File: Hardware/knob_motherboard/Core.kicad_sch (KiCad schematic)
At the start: 20 parts, among them J2 Conn_01x14_Socket, J3 Conn_ARM_SWD_TagConnect_TC203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, U1 ESP32-S3-WROOM-1U, Y2 Crystal_Small

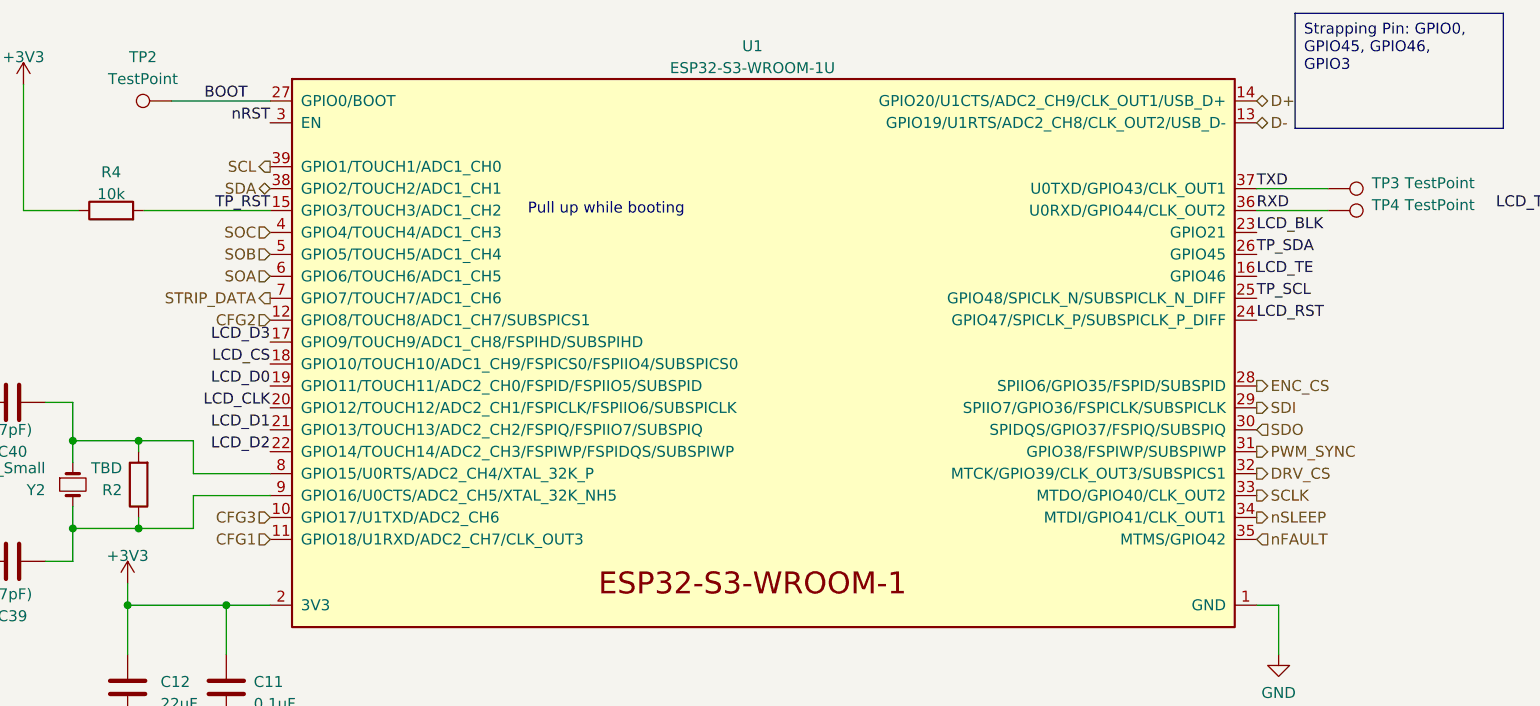
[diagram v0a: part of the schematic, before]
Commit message: drv8311 spi bugfix & ch224k CFG1 bugfix
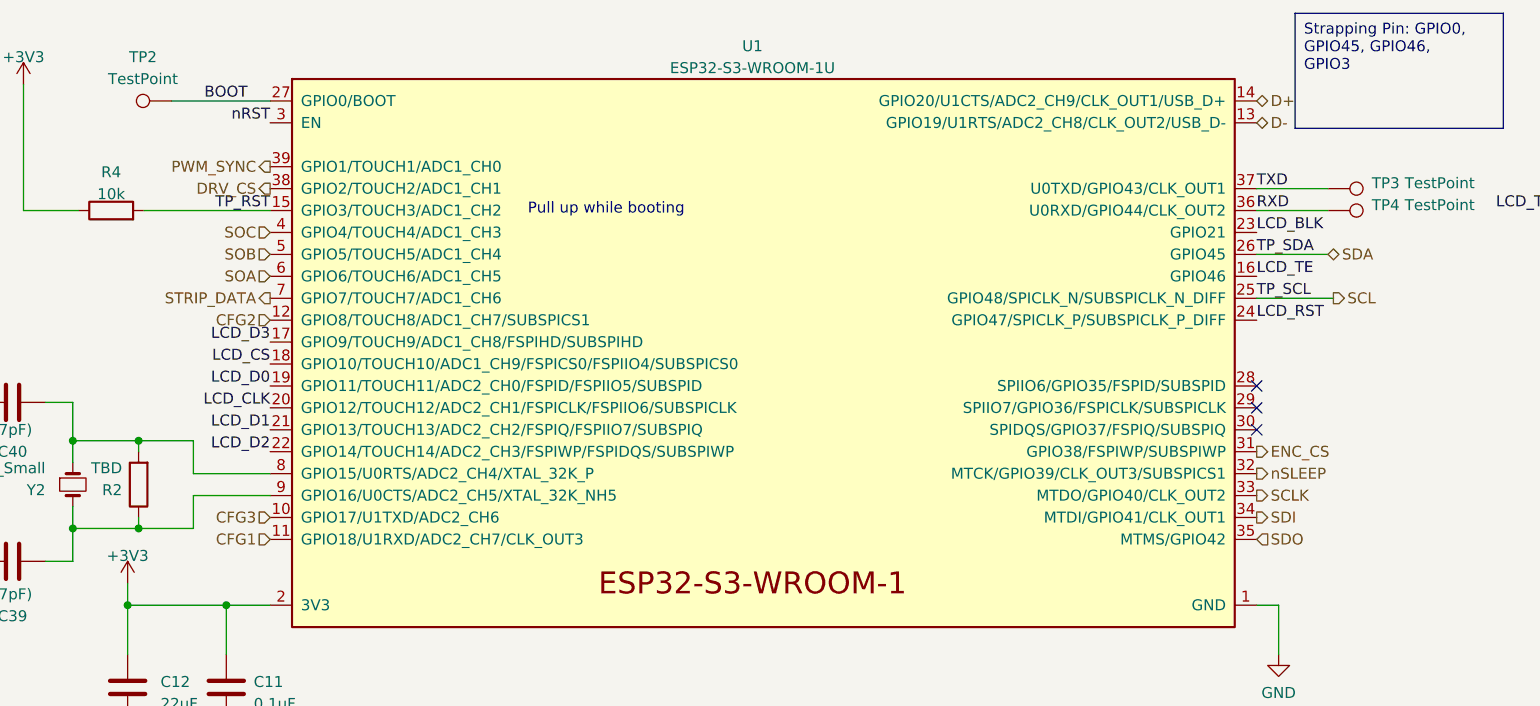
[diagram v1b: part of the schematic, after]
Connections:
- net TP_SCL is gone; now on net SCL: J2.12 (Pin_12), U1.25 (GPIO48/SPICLK_N/SUBSPICLK_N_DIFF)
- net TP_SDA is gone; now on net SDA: J2.13 (Pin_13), U1.26 (GPIO45)
- net nFAULT is gone; now on net SDO: U1.35 (MTMS/GPIO42)
- net DRV_CS: now also U1.38 (GPIO2/TOUCH2/ADC1_CH1); no longer U1.32 (MTCK/GPIO39/CLK_OUT3/SUBSPICS1)
- net ENC_CS: now also U1.31 (GPIO38/FSPIWP/SUBSPIWP); no longer U1.28 (SPIIO6/GPIO35/FSPID/SUBSPID)
- net PWM_SYNC: now also U1.39 (GPIO1/TOUCH1/ADC1_CH0); no longer U1.31 (GPIO38/FSPIWP/SUBSPIWP)
- net SCL: no longer U1.39 (GPIO1/TOUCH1/ADC1_CH0)
- net SDA: no longer U1.38 (GPIO2/TOUCH2/ADC1_CH1)
- net SDI: now also U1.34 (MTDI/GPIO41/CLK_OUT1); no longer U1.29 (SPIIO7/GPIO36/FSPICLK/SUBSPICLK)
- net SDO: no longer U1.30 (SPIDQS/GPIO37/FSPIQ/SUBSPIQ)
- net nSLEEP: now also U1.32 (MTCK/GPIO39/CLK_OUT3/SUBSPICS1); no longer U1.34 (MTDI/GPIO41/CLK_OUT1)
- no-connect marks 0 -> 3
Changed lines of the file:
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@@
   (junction (at 90.17 93.345) (diameter 0) (color 0 0 0 0)
   )
+  (no_connect (at 219.71 79.375))
+  (no_connect (at 219.71 81.915))
+  (no_connect (at 219.71 76.835))
   (wire (pts (xy 93.98 43.815) (xy 105.41 43.815))
     (stroke (width 0) (type default))
   )
+  (wire (pts (xy 228.6 66.675) (xy 219.71 66.675))
+    (stroke (width 0) (type default))
+  )
   (wire (pts (xy 219.71 102.235) (xy 222.25 102.235))
     (stroke (width 0) (type default))
@@
   )
   (wire (pts (xy 90.17 84.455) (xy 90.17 83.185))
+    (stroke (width 0) (type default))
+  )
+  (wire (pts (xy 227.965 61.595) (xy 219.71 61.595))
     (stroke (width 0) (type default))
   )
@@
     (effects (font (size 1.27 1.27)) (justify right))
   )
-  (hierarchical_label "SCL" (shape output) (at 105.41 51.435 180) (fields_autoplaced)
-    (effects (font (size 1.27 1.27)) (justify right))
-  )
-  (hierarchical_label "SDA" (shape bidirectional) (at 105.41 53.975 180) (fields_autoplaced)
-    (effects (font (size 1.27 1.27)) (justify right))
-  )
   (hierarchical_label "CFG2" (shape input) (at 105.41 69.215 180) (fields_autoplaced)
     (effects (font (size 1.27 1.27)) (justify right))
@@
     (effects (font (size 1.27 1.27)) (justify right))
   )
-  (hierarchical_label "DRV_CS" (shape output) (at 219.71 86.995 0) (fields_autoplaced)
-    (effects (font (size 1.27 1.27)) (justify left))
-  )
-  (hierarchical_label "SDI" (shape output) (at 219.71 79.375 0) (fields_autoplaced)
-    (effects (font (size 1.27 1.27)) (justify left))
-  )
-  (hierarchical_label "nFAULT" (shape input) (at 219.71 94.615 0) (fields_autoplaced)
+  (hierarchical_label "DRV_CS" (shape output) (at 105.41 53.975 180) (fields_autoplaced)
+    (effects (font (size 1.27 1.27)) (justify right))
+  )
+  (hierarchical_label "SDI" (shape output) (at 219.71 92.075 0) (fields_autoplaced)
     (effects (font (size 1.27 1.27)) (justify left))
   )
@@
     (effects (font (size 1.27 1.27)) (justify left))
   )
-  (hierarchical_label "PWM_SYNC" (shape output) (at 219.71 84.455 0) (fields_autoplaced)
-    (effects (font (size 1.27 1.27)) (justify left))
+  (hierarchical_label "PWM_SYNC" (shape output) (at 105.41 51.435 180) (fields_autoplaced)
+    (effects (font (size 1.27 1.27)) (justify right))
   )
   (hierarchical_label "SOA" (shape input) (at 105.41 64.135 180) (fields_autoplaced)
     (effects (font (size 1.27 1.27)) (justify right))
   )
-  (hierarchical_label "nSLEEP" (shape output) (at 219.71 92.075 0) (fields_autoplaced)
-    (effects (font (size 1.27 1.27)) (justify left))
-  )
-  (hierarchical_label "SDO" (shape input) (at 219.71 81.915 0) (fields_autoplaced)
+  (hierarchical_label "nSLEEP" (shape output) (at 219.71 86.995 0) (fields_autoplaced)
+    (effects (font (size 1.27 1.27)) (justify left))
+  )
+  (hierarchical_label "SDO" (shape input) (at 219.71 94.615 0) (fields_autoplaced)
     (effects (font (size 1.27 1.27)) (justify left))
   )
@@
     (effects (font (size 1.27 1.27)) (justify right))
   )
-  (hierarchical_label "ENC_CS" (shape output) (at 219.71 76.835 0) (fields_autoplaced)
-    (effects (font (size 1.27 1.27)) (justify left))
-  )
+  (hierarchical_label "SCL" (shape output) (at 228.6 66.675 0) (fields_autoplaced)
+    (effects (font (size 1.27 1.27)) (justify left))
+  )
+  (hierarchical_label "SDA" (shape bidirectional) (at 227.965 61.595 0) (fields_autoplaced)
+    (effects (font (size 1.27 1.27)) (justify left))
+  )
+  (hierarchical_label "ENC_CS" (shape output) (at 219.71 84.455 0) (fields_autoplaced)
+    (effects (font (size 1.27 1.27)) (justify left))
+  )
